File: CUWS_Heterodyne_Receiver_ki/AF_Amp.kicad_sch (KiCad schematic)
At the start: 0 parts

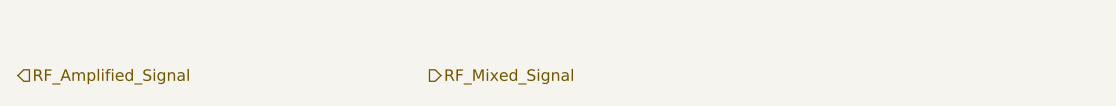
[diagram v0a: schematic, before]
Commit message: Finalised first draft of top hierarchy
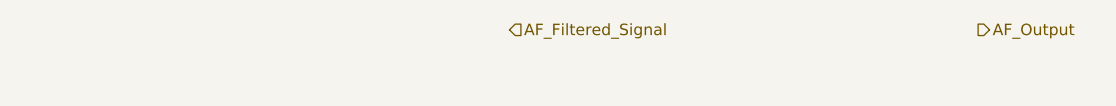
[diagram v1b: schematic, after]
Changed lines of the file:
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@@
 	(generator_version "8.0")
 	(paper "A4")
-	(hierarchical_label "RF_Amplified_Signal"
-		(shape input)
-		(at 50.8 81.28 0)
+	(hierarchical_label "AF_Output"
+		(shape output)
+		(at 157.48 76.2 0)
 		(fields_autoplaced yes)
 		(effects
@@
 		)
 	)
-	(hierarchical_label "RF_Mixed_Signal"
-		(shape output)
-		(at 96.52 81.28 0)
+	(hierarchical_label "AF_Filtered_Signal"
+		(shape input)
+		(at 105.41 76.2 0)
 		(fields_autoplaced yes)
 		(effects

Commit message: Copied Low Pass Filter
OP27 opamp based filter/amp
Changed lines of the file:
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@@
 	(hierarchical_label "AF_Output"
 		(shape output)
-		(at 157.48 76.2 0)
+		(at 177.8 54.61 0)
 		(effects
 			(font
@@
 	(hierarchical_label "AF_Filtered_Signal"
 		(shape input)
-		(at 105.41 76.2 0)
+		(at 88.9 39.37 180)
 		(effects
 			(font
 				(size 1.27 1.27)
 			)
-			(justify left)
+			(justify right)
 		)
 	)

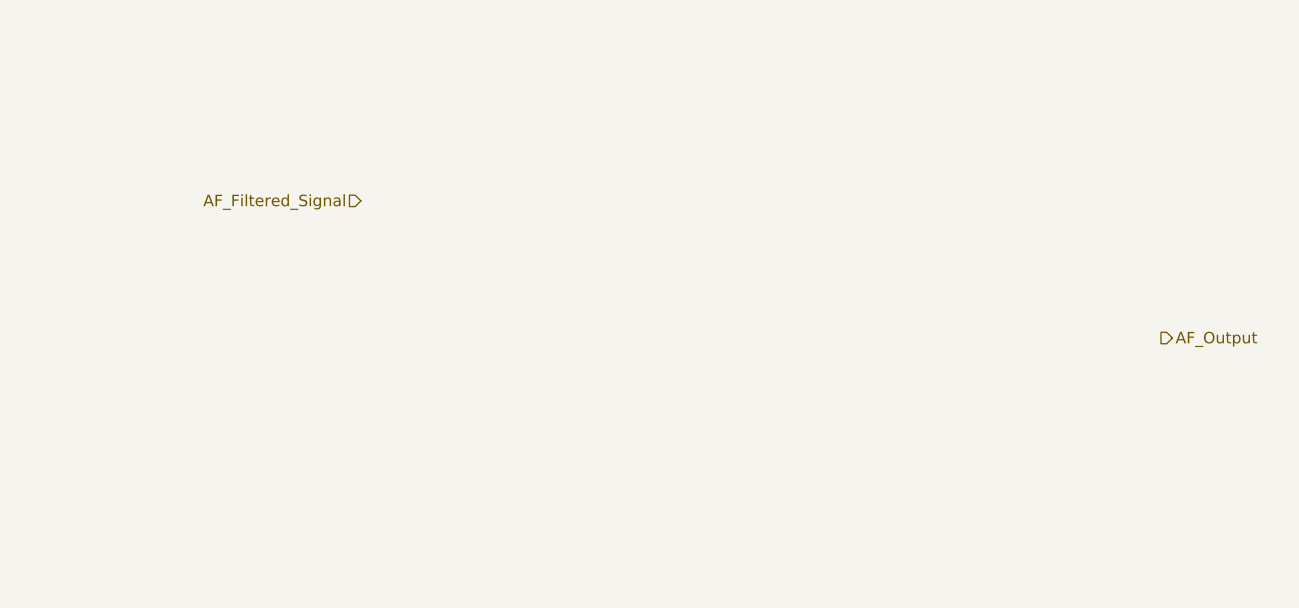
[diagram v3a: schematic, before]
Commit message: Fixing AF Amp stages
Fixed the low pass filter and voltage OpAmp circuit, followed by a push-pull current amp.
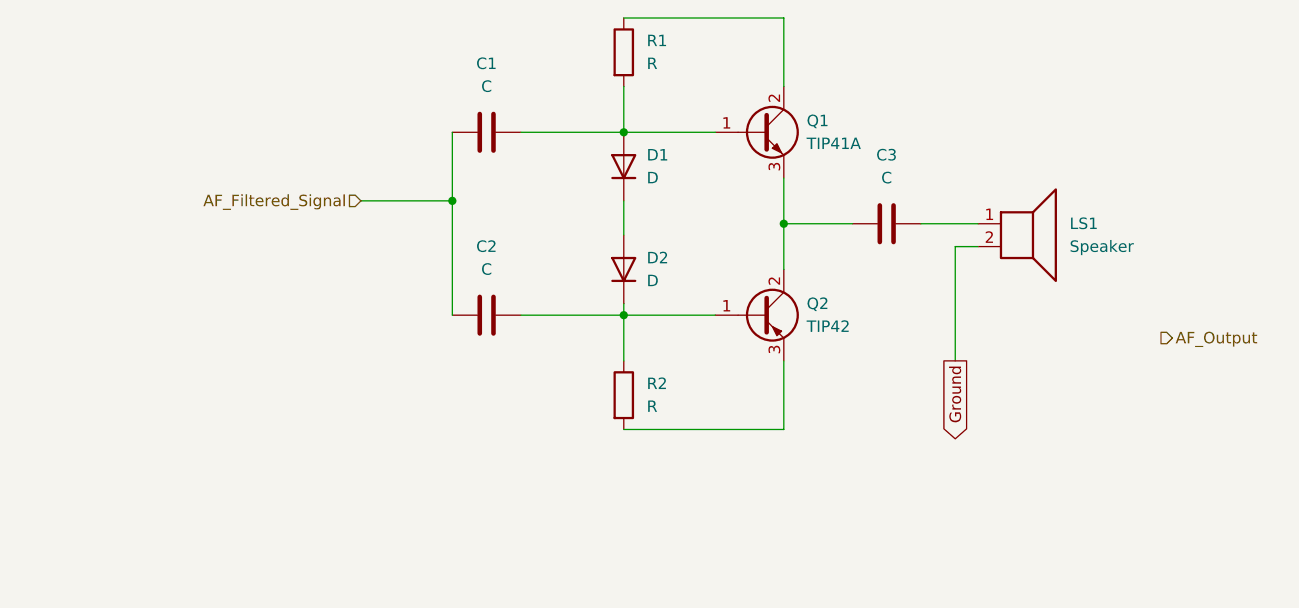
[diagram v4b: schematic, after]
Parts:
- added C1, C2, C3: C, symbol Device:C
- added D1, D2: D, symbol Device:D
- added LS1: Speaker, symbol Device:Speaker
- added Q1: TIP41A, Package_TO_SOT_THT:TO-220-3_Vertical, symbol Transistor_BJT:TIP41A
- added Q2: TIP42, Package_TO_SOT_THT:TO-220-3_Vertical, symbol Transistor_BJT:TIP42
- added R1, R2: R, symbol Device:R
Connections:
- net AF_Filtered_Signal: now also C1.2, C2.1
- new net: C2.2, D2.1 (K), Q2.1 (B), R2.1
- new net: C3.1, Q1.3 (E), Q2.2 (C)
- new net: Q2.3 (E), R2.2
- new net: D1.1 (K), D2.2 (A)
- new net: Q1.2 (C), R1.1
- new net: C1.1, D1.2 (A), Q1.1 (B), R1.2
- new net: C3.2, LS1.1
- new net Ground: LS1.2
